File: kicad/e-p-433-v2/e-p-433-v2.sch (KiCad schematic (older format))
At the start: 20 parts, among them P3 ant, P5 Transmitter, SW1 Capuchon vert, SW2 SW_PUSH_m, U3 Teensy_3-2

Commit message: Mise à jour du 16 mars 2018
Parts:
- removed W4: 3.3V, Sp:Measurement_Point_Square-SMD-Pad_Big, symbol TEST_1P
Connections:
- wire segments 40 -> 41

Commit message: Ajout de fichiers et modification de fichiers de la e-p-433-v2
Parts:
- added P?: Transmitter, Connect:PINHEAD1-6, symbol e-p-433-v2-rescue:CONN_01X06
- C5: symbol C -> e-p-433-v2-rescue:C
- D1, D3, D4: symbol LED -> e-p-433-v2-rescue:LED-RESCUE-e-p-433-v2
- P3: symbol CONN_01X01 -> e-p-433-v2-rescue:CONN_01X01
- P5: symbol CONN_01X06 -> e-p-433-v2-rescue:CONN_01X06
- R10, R11, R12, R13, R14, R16, R17, R7, R8, R9: symbol R -> e-p-433-v2-rescue:R
- SW1: symbol Capuchon -> Sp:Capuchon
- SW2: symbol SW_PUSH_m -> Sp:SW_PUSH_m
- U3: symbol Teensy_3-2 -> Sp:Teensy_3-2
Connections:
- wire segments 41 -> 53
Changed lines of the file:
@@
-EESchema Schematic File Version 2
-LIBS:power
-LIBS:device
-LIBS:transistors
-LIBS:conn
-LIBS:linear
-LIBS:regul
-LIBS:74xx
-LIBS:cmos4000
-LIBS:adc-dac
-LIBS:memory
-LIBS:xilinx
-LIBS:microcontrollers
-LIBS:dsp
-LIBS:microchip
-LIBS:analog_switches
-LIBS:motorola
-LIBS:texas
-LIBS:intel
-LIBS:audio
-LIBS:interface
-LIBS:digital-audio
-LIBS:philips
-LIBS:display
-LIBS:cypress
-LIBS:siliconi
-LIBS:opto
-LIBS:atmel
-LIBS:contrib
-LIBS:valves
-LIBS:Sp
+EESchema Schematic File Version 4
 LIBS:e-p-433-v2-cache
-EELAYER 25 0
+EELAYER 26 0
 EELAYER END
 $Descr A4 11693 8268
@@
 $EndDescr
 $Comp
-L CONN_01X06 P5
+L e-p-433-v2-rescue:CONN_01X06 P5
 U 1 1 58025B97
 P 9820 1305
@@
 $Bitmap
 Pos 9625 6825
-Scale 0,100000
+Scale 0.000000
 Data
 89 50 4E 47 0D 0A 1A 0A 00 00 00 0D 49 48 44 52 00 00 0F 81 00 00 05 90 08 02 00 00 00 61 88 44
@@
 00 00 00 00 E0 72 D0 01 00 00 00 00 00 00 00 00 00 00 B8 1C 74 00 00 00 00 00 00 00 00 00 00 00
 2E 07 1D 00 00 00 00 00 00 00 00 00 00 80 2B 9B 72 A2 EA 82 B7 AD 55 00 00 00 00 49 45 4E 44 AE
-42 60 82 00
+42 60 82
 EndData
 $EndBitmap
@@
 3 X diviseur par 2
 $Comp
-L LED D3
+L e-p-433-v2-rescue:LED-RESCUE-e-p-433-v2 D3
 U 1 1 580638D6
 P 7835 2465
@@
 $EndComp
 $Comp
-L LED D4
+L e-p-433-v2-rescue:LED-RESCUE-e-p-433-v2 D4
 U 1 1 58063C6E
 P 8135 2465
@@
 $EndComp
 $Comp
-L LED D1
+L e-p-433-v2-rescue:LED-RESCUE-e-p-433-v2 D1
 U 1 1 58063F1D
 P 7535 2465
@@
 Data to transmiter
 $Comp
-L 3.3V #PWR17
+L Sp:3.3V #PWR17
 U 1 1 582B4AFD
 P 9445 1355
@@
 $EndComp
 $Comp
-L 3.3V #PWR13
+L Sp:3.3V #PWR13
 U 1 1 582B5D56
 P 3350 2895
@@
 T1
 $Comp
-L C C5
+L e-p-433-v2-rescue:C C5
 U 1 1 582C67BB
 P 3350 3230
@@
 $EndComp
 $Comp
-L VBAT #PWR11
+L Sp:VBAT #PWR11
 U 1 1 582CBA63
 P 3760 3065
@@
 $EndComp
 $Comp
-L VUSB #PWR10
+L Sp:VUSB #PWR10
 U 1 1 582F4DB9
 P 3710 3765
@@
 $EndComp
 $Comp
-L R R13
+L e-p-433-v2-rescue:R R13
 U 1 1 5832F0E0
 P 5735 2740
@@
 $EndComp
 $Comp
-L R R8
+L e-p-433-v2-rescue:R R8
 U 1 1 5832F4F4
 P 5135 2140
@@
 $EndComp
 $Comp
-L R R9
+L e-p-433-v2-rescue:R R9
 U 1 1 5832F6EF
 P 5435 2140
@@
 $EndComp
 $Comp
-L R R11
+L e-p-433-v2-rescue:R R11
 U 1 1 5832F908
 P 5735 2140
@@
 $EndComp
 $Comp
-L R R14
+L e-p-433-v2-rescue:R R14
 U 1 1 5832FAF1
 P 7535 2015
@@
 $EndComp
 $Comp
-L R R12
+L e-p-433-v2-rescue:R R12
 U 1 1 58330094
 P 5435 2740
@@
 $EndComp
 $Comp
-L R R10
+L e-p-433-v2-rescue:R R10
 U 1 1 58330234
 P 5135 2740
@@
 	9870 1605 9870 1005
 $Comp
-L Teensy_3-2 U3
+L Sp:Teensy_3-2 U3
 U 1 1 583882A5
 P 6185 4215
@@
 $EndComp
 $Comp
-L GND #PWR9
+L power:GND #PWR9
 U 1 1 583C8ED8
 P 4260 5640
@@
 $EndComp
 $Comp
-L GND #PWR18
+L power:GND #PWR18
 U 1 1 583C9DE2
 P 9620 1555
@@
 $EndComp
 $Comp
-L GND #PWR12
+L power:GND #PWR12
 U 1 1 583C80AA
 P 8310 1865
@@
 $EndComp
 $Comp
-L R R16
+L e-p-433-v2-rescue:R R16
 U 1 1 58407AA4
 P 7835 2015
@@
 $EndComp
 $Comp
-L R R17
+L e-p-433-v2-rescue:R R17
 U 1 1 58407F65
 P 8135 2015
@@
 	9445 1355 9620 1355
 $Comp
-L Capuchon SW1
+L Sp:Capuchon SW1
 U 1 1 5845B03C
 P 7960 5665
@@
 $EndComp
 $Comp
-L 3.3V #PWR7
+L Sp:3.3V #PWR7
 U 1 1 5845BA73
 P 8135 5965
@@
 $EndComp
 $Comp
-L R R7
+L e-p-433-v2-rescue:R R7
 U 1 1 5845BAE5
 P 8285 5365
@@
 $EndComp
 $Comp
-L GND #PWR8
+L power:GND #PWR8
 U 1 1 5845BB66
 P 8435 5365
@@
 $EndComp
 $Comp
-L SW_PUSH_m SW2
+L Sp:SW_PUSH_m SW2
 U 1 1 58483BFB
 P 8135 5665
@@
 Connection ~ 8135 5365
 $Comp
-L CONN_01X01 P3
+L e-p-433-v2-rescue:CONN_01X01 P3
 U 1 1 5899B57D
 P 9520 855
@@
 $EndComp
 Wire Wire Line
-	8285 5765 8285 5515
+	8285 5765 8285 5565
 Wire Wire Line
 	8285 5515 8435 5515
@@
 Connection ~ 8285 5565
 Wire Wire Line
-	6935 3065 6935 2840
-Wire Wire Line
-	7235 2740 7235 3065
-Wire Wire Line
-	4535 3765 3710 3765
+	4535 3765 4010 3765
 Connection ~ 4010 3765
 Wire Wire Line
@@
 	5735 3065 5735 2890
 Wire Wire Line
-	4835 3065 4835 2590
+	4835 3065 4835 2895
 Wire Wire Line
 	4835 2590 5135 2590
 Wire Wire Line
-	5435 2590 5435 2290
+	5435 2590 5435 2515
 Wire Wire Line
 	4010 2515 5435 2515
 Wire Wire Line
-	5735 2590 5735 2290
+	5735 2590 5735 2415
 Wire Wire Line
 	5135 2590 5135 2290
@@
 Wire Wire Line
 	5135 1990 5135 1940
-Connection ~ 5135 1940
 Wire Wire Line
-	5435 1990 5435 1735
+	5435 1990 5435 1940
 Connection ~ 5435 1940
 Wire Wire Line
@@
 	8135 2265 8135 2165
 Wire Wire Line
-	7535 1865 8310 1865
+	7535 1865 7835 1865
 Connection ~ 7835 1865
 Connection ~ 8135 1865
@@
 	5820 3460 4925 3460
 Wire Wire Line
-	9620 1055 9620 1255
+	9620 1055 9620 1155
 Connection ~ 9620 1155
 Wire Wire Line
 	9620 1055 9520 1055
 $Comp
-L GND #PWR?
+L power:GND #PWR?
 U 1 1 59958A01
 P 5435 1735
@@
 $EndComp
 Wire Wire Line
-	5135 1940 5735 1940
+	5135 1940 5435 1940
 Wire Notes Line
 	5820 1345 4925 1345
 $Comp
-L GND #PWR?
+L power:GND #PWR?
 U 1 1 59959D4F
 P 3350 3380
@@
 Wire Wire Line
 	3350 2900 3355 2900
+Wire Wire Line
+	8285 5565 8285 5515
+Wire Wire Line
+	4010 3765 3710 3765
+Wire Wire Line
+	5435 2515 5435 2290
+Wire Wire Line
+	5735 2415 5735 2290
+Wire Wire Line
+	5435 1940 5435 1735
+Wire Wire Line
+	5435 1940 5735 1940
+Wire Wire Line
+	7835 1865 8135 1865
+Wire Wire Line
+	8135 1865 8310 1865
+Wire Wire Line
+	9620 1155 9620 1255
+Wire Wire Line
+	4835 2895 4835 2590
+$Comp
+L e-p-433-v2-rescue:CONN_01X06 P?
+U 1 1 5C3AD164
+P 7925 945
+F 0 "P?" V 7925 1320 50  0000 C CNN
+F 1 "Transmitter" H 8230 1320 60  0000 C CNB
+F 2 "Connect:PINHEAD1-6" H 7925 945 50  0001 C CNN
+F 3 "https://cdn.sparkfun.com/datasheets/Prototyping/SP-140520-XX-001.pdf" H 7925 945 50  0001 C CNN
+F 4 "Arduino 6-Pin Stackable Headers" H 7925 945 60  0001 C CNN "Désignation"
+F 5 "GCT" H 7925 945 60  0001 C CNN "Fabricant"
+F 6 "SP-140520-06-001" H 7925 945 60  0001 C CNN "Ref-fab"
+F 7 "Sparkfun" H 7925 945 60  0001 C CNN "Distributeur"
+F 8 "PRT09280" H 7925 945 60  0001 C CNN "Ref-distri"
+F 9 "0,50 €" H 7925 945 60  0001 C CNN "Prix"
+	1    7925 945
+	1    0    0    1
+$EndComp
+Wire Wire Line
+	6935 795  7725 795
+Wire Wire Line
+	6935 795  6935 3065
+Wire Wire Line
+	7725 1095 7235 1095
+Wire Wire Line
+	7235 1095 7235 3065
 $EndSCHEMATC

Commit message: Modification des fichiers e-p-433-v2.*
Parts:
- removed P?: Transmitter, Connect:PINHEAD1-6, symbol e-p-433-v2-rescue:CONN_01X06
- added J?: 2 X thermomètre digital, symbol Connector_Generic:Conn_01x08
- added R? (x2): 47K, symbol Device:R
- added R?: 1 OHM, symbol Device:R
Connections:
- net labels added: VBAT1
- net labels removed: VBAT
- wire segments 53 -> 75
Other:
- note added: "2 X DS 18B 2O"
- note added: "DQ"
- note added: "Entretoise de fixation [16]"
- note added: "Interface des thermomètres digitaux"
- note added: "Méplat"
- note added: "T1 -> Teensy 3.2 (D17)"
- note added: "T2 -> Teensy 3.2 (D16)"
- note added: "VDD"
- note added: "batterie"
- note added: "couvercle"
- moved on the sheet: C5, D1, D3, D4, P3, P5, R10, R11, R12, R13, R14, R16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

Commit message: Reprise de kicad
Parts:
- added BT1: Batterie LI-ION PRT-13851, symbol Device:Battery_Cell
- added R10, R11: 4.7K, Resistors_SMD:R_0603, symbol e-p-433-v2-rescue:R
- added SW1: SW_DPDT_x2, symbol Switch:SW_DPDT_x2
- added U1: PRT-10401, symbol Sp:PRT-10401
- gave numbers to parts that had none: 4
- renumbered C5 to C1, D3 to D2, D4 to D3, P3 to P1, P5 to P2, R14 to R12, R16 to R13, R17 to R14, R7 to R15, R8 to R4, R10 to R5, R9 to R6, R12 to R7, R11 to R8, R13 to R9, SW1 to SW2, SW2 to SW3, U3 to U2
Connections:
- net +5V: now also U1.~ (Vusb-)
- net +BATT: now also R8.1, R9.1, U2.D12, U2.VIN (3.6-to-6.0-V-), U2.Vbat, BT1.1 (+), R10.2, R11.1, SW1.3 (C), U1.~ (Vusb-)
- net 3.3V: now also SW3.2; no longer SW3.1
- net GND: now also BT1.2 (-), R10.1, U1.~ (Vusb-)
- net at U2.D11: now also R15.1, SW3.1
- net at J1.2 (Pin_2), U2.D16 (A2): now also R3.2
- net at J1.7 (Pin_7), R2.2, U2.D17 (A3): no longer R3.2
- net at U2.D20 (A6): now also R11.2
- new net: R1.2, SW1.2 (B)
- no-connect marks 17 -> 15
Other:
- note added: "4 X diviseur par 2"
- note added: "Alimentation permanente de l'horloge"
- note added: "Chargeur"
- note added: "VBAT1"
- note added: "VBAT2"
- note removed: "3 X diviseur par 2"
- note removed: "VBAT"
- moved on the sheet: R1, R15, SW2, SW3

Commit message: Mise à jour de fichiers Kicad
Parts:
- removed SW1: SW_DPDT_x2, symbol Switch:SW_DPDT_x2
- removed SW2: Capuchon vert, Sp:Capuchon, symbol Sp:Capuchon
- removed SW3: SW_PUSH_m, Sp:SW_Micro_SPST_Angled, symbol Sp:SW_PUSH_m
- added D1: Verte, LEDs:LED_0603, symbol e-p-433-v2-rescue:LED-RESCUE-e-p-433-v2
- added D2: Bleue, LEDs:LED_0603, symbol e-p-433-v2-rescue:LED-RESCUE-e-p-433-v2
- added R2, R3: 47K, Resistors_SMD:R_0603, symbol e-p-433-v2-rescue:R
- added R4: 1K, Resistors_SMD:R_0603, symbol e-p-433-v2-rescue:R
- added SW1, SW2, SW3: SW_SPDT, symbol Switch:SW_SPDT
- added Y1: Cristal, 32.768 kHz, symbol Device:Crystal
- R15: value 47K -> 1K; Distributeur CONRAD -> Conrad; Désignation Résistance à couche épaisse 47 kΩ CMS 0603 0.1 W 5 % 100 ±p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 -> Résistance à couche épaisse 1 kΩ CMS 0603 0.1 W 5 %; Ref-distri 1457808 - 62 -> 1457724 - 62; Ref-fab 0603SAJ0473T5E -> 0603SAJ0102T5E
- renumbered D1 to D3, D2 to D4, D3 to D5, R7 to R10, R8 to R11, R9 to R12, R10 to R13, R11 to R14, R12 to R16, R13 to R17, R14 to R18, R2 to R5, R3 to R6, R4 to R7, R5 to R8, R6 to R9
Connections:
- net +BATT: now also R1.2, D1.2 (A), SW1.3 (C); no longer R1.1
- net 3.3V: now also SW2.2 (B), SW3.2 (B)
- net GND: now also R2.2, R3.2, R4.2
- net at U2.D10: now also R3.1, SW2.3 (C)
- net at U2.D11: now also R2.1, SW3.3 (C); no longer R15.1
- net at U2.D19 (A5): now also D2.2 (A)
- net at U2.~ (XTAL32): now also Y1.2
- new net: U2.~ (XTAL32), Y1.1
- new net: R1.1, SW1.2 (B)
- new net: D2.1 (K), R15.1
- new net: D1.1 (K), R4.1
- no-connect marks 15 -> 14
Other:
- note added: "Breadboard [3b]"
- note added: "Fichiers associés :\nSCAO/kicad/e-p-433-v2/e-p-433-v2.pdf (-> impression)\nSCAO/kicad/e-p-433-v2/e-p-433-v2-1.png (-> wiki)\nSCAO/kicad/e-p-433-v2/e-p-433-v2-2.png (-> wiki - interface des themomètres digitaux)"
- note added: "IHM"
- note added: "Mesure de ibat"
- note added: "StSp"
- note added: "[17]"
- note added: "[3d]"
- note added: "[4]"
- note added: "[7]"
- note added: "sleep"
- note removed: "VBAT1"
- note removed: "batterie"
- note removed: "couvercle"
- moved on the sheet: R1

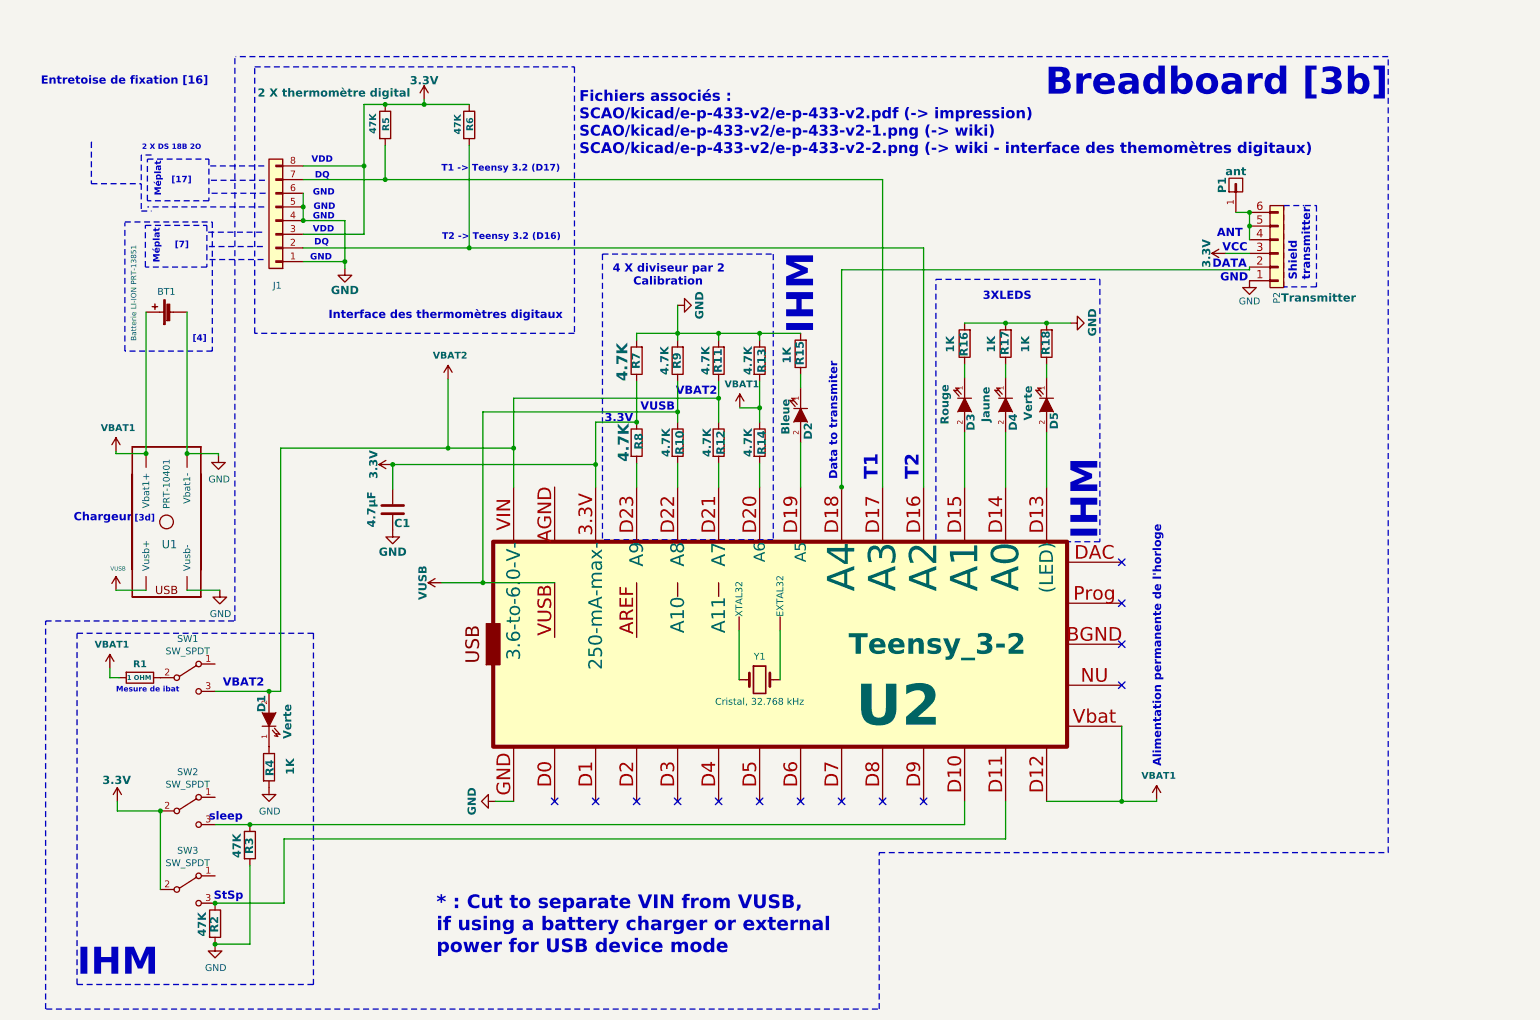
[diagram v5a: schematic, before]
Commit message: Modification du cahier des charges et du schéma électrique
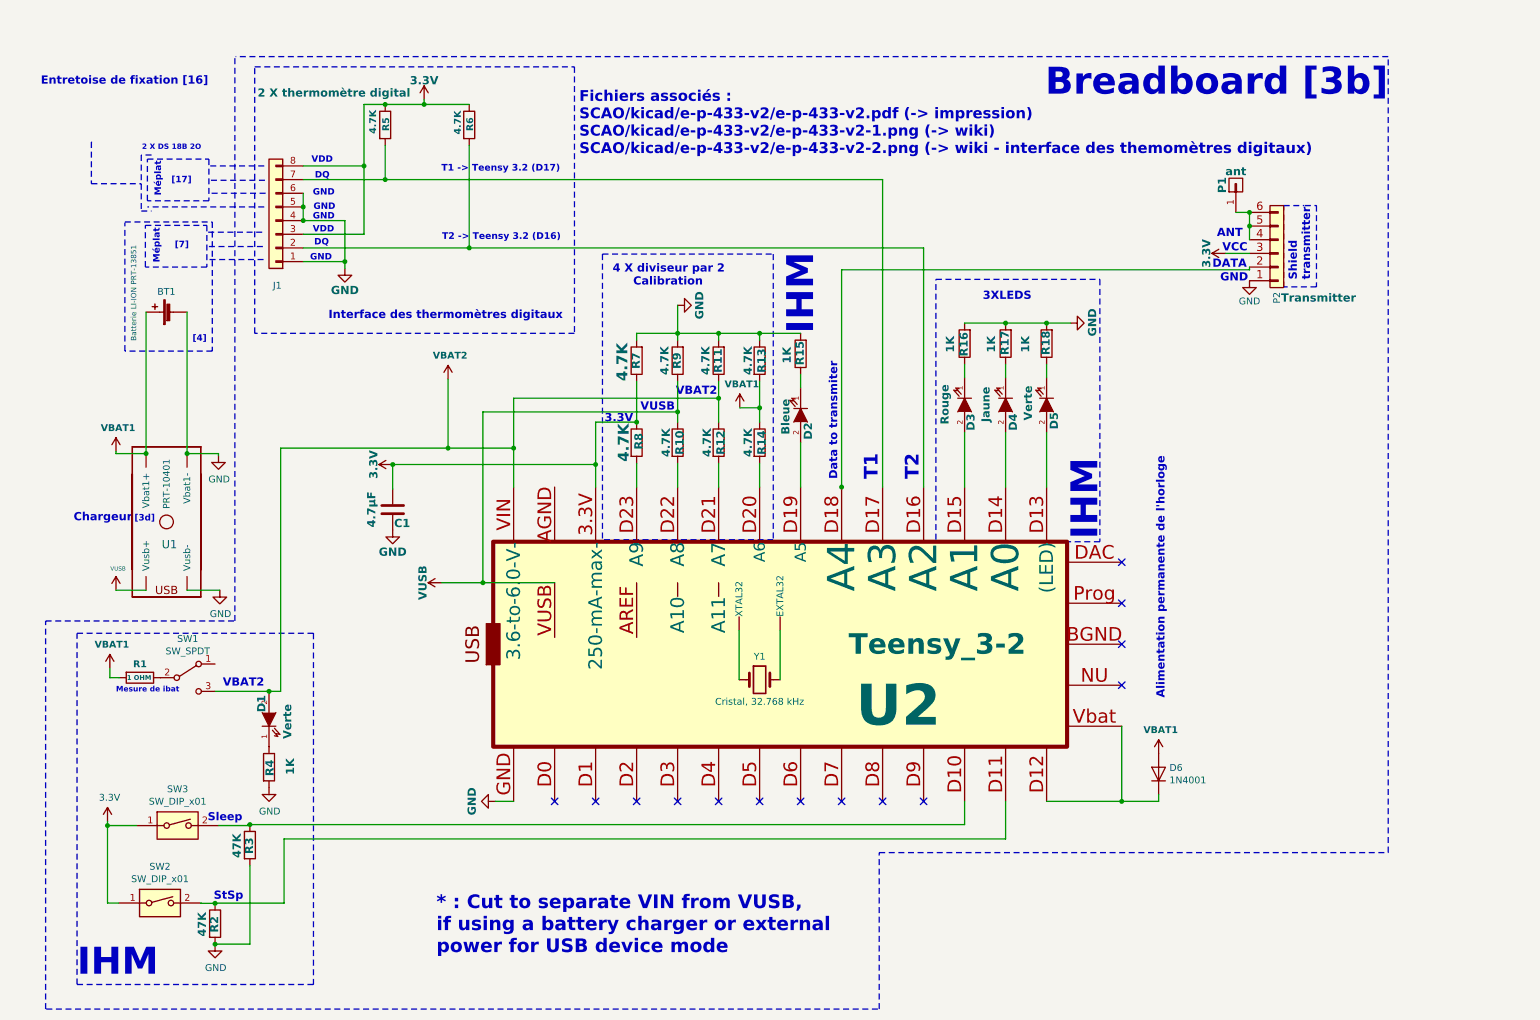
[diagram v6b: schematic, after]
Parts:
- removed SW2, SW3: SW_SPDT, symbol Switch:SW_SPDT
- added D6: 1N4001, Diode_THT:D_DO-41_SOD81_P10.16mm_Horizontal, symbol Diode:1N4001
- added SW2, SW3: SW_DIP_x01, symbol Switch:SW_DIP_x01
- R5, R6: value 47K -> 4.7K
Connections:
- net +BATT: now also D6.2 (A); no longer U2.D12, U2.Vbat
- net 3.3V: now also SW2.1, SW3.1
- net at R3.1, U2.D10: now also SW3.2
- net at R2.1, U2.D11: now also SW2.2
- net at U2.~ (XTAL32): now also Y1.2
- new net: D6.1 (K), U2.D12, U2.Vbat
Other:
- note added: "Sleep"
- note removed: "sleep"
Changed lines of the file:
@@
 EESchema Schematic File Version 4
 LIBS:e-p-433-v2-cache
-EELAYER 26 0
+EELAYER 29 0
 EELAYER END
 $Descr A4 11693 8268
@@
 $Bitmap
 Pos 9625 6825
-Scale 0.000000
+Scale 0.150000
 Data
 89 50 4E 47 0D 0A 1A 0A 00 00 00 0D 49 48 44 52 00 00 0F 81 00 00 05 90 08 02 00 00 00 61 88 44
@@
 P 3240 1100
 F 0 "R5" V 3245 1055 50  0000 L CNB
-F 1 "47K" V 3150 1035 50  0000 L CNB
+F 1 "4.7K" V 3150 1035 50  0000 L CNB
 F 2 "" V 3170 1100 50  0001 C CNN
 F 3 "~" H 3240 1100 50  0001 C CNN
@@
 P 3855 1100
 F 0 "R6" V 3860 1055 50  0000 L CNB
-F 1 "47K" V 3770 1030 50  0000 L CNB
+F 1 "4.7K" V 3770 1030 50  0000 L CNB
 F 2 "" V 3785 1100 50  0001 C CNN
 F 3 "~" H 3855 1100 50  0001 C CNN
@@
 L Sp:VBAT1 #PWR019
 U 1 1 5C4C1E96
-P 8885 6035
-F 0 "#PWR019" H 8885 5885 50  0001 C CNN
-F 1 "VBAT1" H 8900 6208 50  0000 C CNB
-F 2 "" H 8885 6035 50  0000 C CNN
-F 3 "" H 8885 6035 50  0000 C CNN
-	1    8885 6035
+P 8900 5700
+F 0 "#PWR019" H 8900 5550 50  0001 C CNN
+F 1 "VBAT1" H 8915 5873 50  0000 C CNB
+F 2 "" H 8900 5700 50  0000 C CNN
+F 3 "" H 8900 5700 50  0000 C CNN
+	1    8900 5700
 	1    0    0    -1
 $EndComp
 Wire Wire Line
-	8080 6050 8630 6050
-Wire Wire Line
-	8885 6050 8885 6035
-Wire Wire Line
 	8630 5500 8630 6050
-Connection ~ 8630 6050
-Wire Wire Line
-	8630 6050 8885 6050
-Text Notes 8925 5800 1    60   ~ 12
+Text Notes 8950 5300 1    60   ~ 12
 Alimentation permanente de l'horloge
 Text Notes 960  4010 0    60   ~ 12
@@
 Text Notes 1985 6780 0    60   ~ 12
 StSp
-Text Notes 1950 6200 0    60   ~ 12
-sleep
-$Comp
-L Switch:SW_SPDT SW1
-U 1 1 5C5AAEFC
-P 1795 5145
-F 0 "SW1" H 1795 5430 50  0000 C CNN
-F 1 "SW_SPDT" H 1795 5339 50  0000 C CNN
-F 2 "" H 1795 5145 50  0001 C CNN
-F 3 "" H 1795 5145 50  0001 C CNN
-	1    1795 5145
-	1    0    0    -1
-$EndComp
-$Comp
-L Switch:SW_SPDT SW2
-U 1 1 5C4F8866
-P 1795 6120
-F 0 "SW2" H 1795 6405 50  0000 C CNN
-F 1 "SW_SPDT" H 1795 6314 50  0000 C CNN
-F 2 "" H 1795 6120 50  0001 C CNN
-F 3 "" H 1795 6120 50  0001 C CNN
-	1    1795 6120
-	1    0    0    -1
-$EndComp
-$Comp
-L Switch:SW_SPDT SW3
-U 1 1 5C4F89F9
-P 1795 6695
-F 0 "SW3" H 1795 6980 50  0000 C CNN
-F 1 "SW_SPDT" H 1795 6889 50  0000 C CNN
-F 2 "" H 1795 6695 50  0001 C CNN
-F 3 "" H 1795 6695 50  0001 C CNN
-	1    1795 6695
-	1    0    0    -1
-$EndComp
-$Comp
-L Sp:3.3V #PWR04
-U 1 1 5C4FC997
-P 1280 6050
-F 0 "#PWR04" H 1280 5900 50  0001 C CNN
-F 1 "3.3V" H 1275 6205 60  0000 C CNB
-F 2 "" H 1280 6050 50  0000 C CNN
-F 3 "" H 1280 6050 50  0000 C CNN
-	1    1280 6050
-	1    0    0    -1
-$EndComp
-Wire Wire Line
-	1595 6120 1280 6120
-Wire Wire Line
-	1280 6120 1280 6050
-Wire Wire Line
-	1595 6695 1595 6120
-Connection ~ 1595 6120
 $Comp
 L e-p-433-v2-rescue:R R2
@@
 Connection ~ 1995 7095
 Wire Wire Line
-	1995 6220 2250 6220
-Wire Wire Line
 	4045 6050 4180 6050
 Wire Wire Line
@@
 Wire Wire Line
 	7480 6220 7480 6050
-Connection ~ 2250 6220
 Wire Wire Line
 	7780 6050 7780 6325
@@
 Wire Wire Line
 	2500 6795 1995 6795
-Connection ~ 1995 6795
 Wire Wire Line
 	2250 6520 2250 7095
@@
 Wire Notes Line width 39 style solid
 	2140 4730 2140 605
+$Comp
+L Diode:1N4001 D6
+U 1 1 5CABF9CF
+P 8900 5850
+F 0 "D6" V 8946 5771 50  0000 R CNN
+F 1 "1N4001" V 8855 5771 50  0000 R CNN
+F 2 "Diode_THT:D_DO-41_SOD81_P10.16mm_Horizontal" H 8900 5675 50  0001 C CNN
+F 3 "http://www.vishay.com/docs/88503/1n4001.pdf" H 8900 5850 50  0001 C CNN
+	1    8900 5850
+	0    -1   -1   0
+$EndComp
+Wire Wire Line
+	8900 6000 8900 6050
+Wire Wire Line
+	8080 6050 8630 6050
+Connection ~ 8630 6050
+Wire Wire Line
+	8630 6050 8900 6050
+$Comp
+L Switch:SW_SPDT SW1
+U 1 1 5C5AAEFC
+P 1795 5145
+F 0 "SW1" H 1795 5430 50  0000 C CNN
+F 1 "SW_SPDT" H 1795 5339 50  0000 C CNN
+F 2 "" H 1795 5145 50  0001 C CNN
+F 3 "" H 1795 5145 50  0001 C CNN
+	1    1795 5145
+	1    0    0    -1
+$EndComp
+$Comp
+L Switch:SW_DIP_x01 SW3
+U 1 1 5CB1A3E8
+P 1721 6227
+F 0 "SW3" H 1721 6494 50  0000 C CNN
+F 1 "SW_DIP_x01" H 1721 6403 50  0000 C CNN
+F 2 "" H 1721 6227 50  0001 C CNN
+F 3 "~" H 1721 6227 50  0001 C CNN
+	1    1721 6227
+	1    0    0    -1
+$EndComp
+$Comp
+L Switch:SW_DIP_x01 SW2
+U 1 1 5CB5D7C7
+P 1592 6794
+F 0 "SW2" H 1592 7061 50  0000 C CNN
+F 1 "SW_DIP_x01" H 1592 6970 50  0000 C CNN
+F 2 "" H 1592 6794 50  0001 C CNN
+F 3 "~" H 1592 6794 50  0001 C CNN
+	1    1592 6794
+	1    0    0    -1
+$EndComp
+$Comp
+L Sp:3.3V #PWR04
+U 1 1 5CB20CF7
+P 1208 6195
+F 0 "#PWR04" H 1208 6045 50  0001 C CNN
+F 1 "3.3V" H 1223 6368 50  0000 C CNN
+F 2 "" H 1208 6195 50  0000 C CNN
+F 3 "" H 1208 6195 50  0000 C CNN
+	1    1208 6195
+	1    0    0    -1
+$EndComp
+Wire Wire Line
+	1421 6227 1208 6227
+Wire Wire Line
+	2021 6227 2236 6227
+Wire Wire Line
+	2236 6227 2236 6220
+Wire Wire Line
+	2236 6220 2250 6220
+Connection ~ 2250 6220
+Wire Wire Line
+	1292 6794 1208 6794
+Wire Wire Line
+	1208 6195 1208 6227
+Connection ~ 1208 6227
+Wire Wire Line
+	1208 6227 1208 6794
+Wire Wire Line
+	1995 6795 1995 6796
+Wire Wire Line
+	1995 6796 1892 6796
+Wire Wire Line
+	1892 6796 1892 6794
+Connection ~ 1995 6796
+Wire Wire Line
+	1995 6796 1995 6799
+Text Notes 1941 6205 0    59   ~ 12
+Sleep
 $EndSCHEMATC
